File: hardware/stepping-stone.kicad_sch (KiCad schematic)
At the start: 0 parts

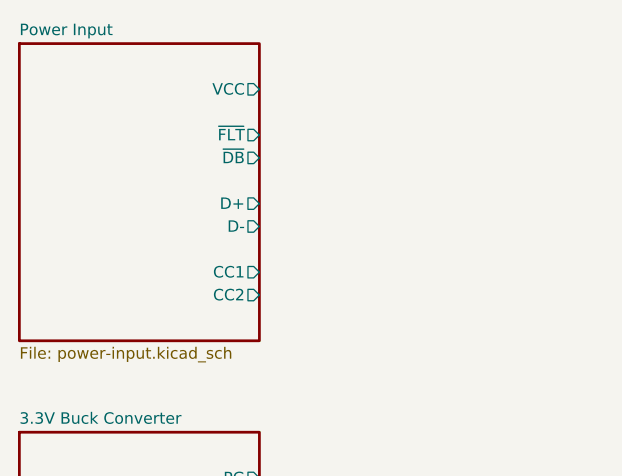
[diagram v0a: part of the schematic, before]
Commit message: Remove USB C PD and refine power input
Deleted USB C PD features due to complexity. Simplified power input schematic. Sourced PSU, connectors, crimps, and created external harness schematics.
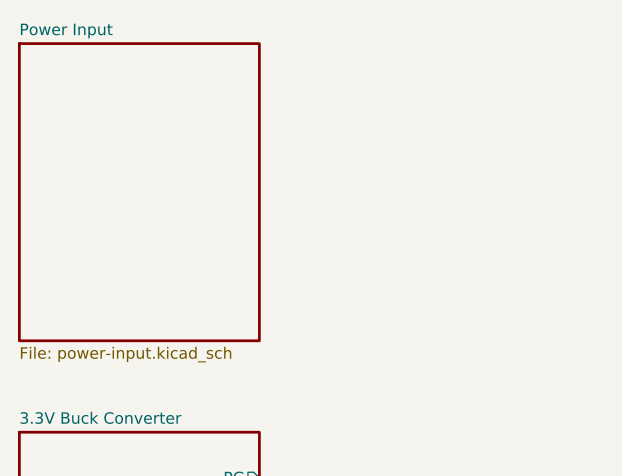
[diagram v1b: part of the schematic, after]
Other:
- sheet Power Input ports: added none; removed CC1, CC2, D+, D-, VCC, ~{DB}, ~{FLT}
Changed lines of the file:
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@@
-			)
-		)
-		(pin "CC1" output
-			(at 68.58 50.8 0)
-			(effects
-				(font
-					(size 1.27 1.27)
-				)
-				(justify right)
-			)
-		)
-		(pin "CC2" output
-			(at 68.58 53.34 0)
-			(effects
-				(font
-					(size 1.27 1.27)
-				)
-				(justify right)
-			)
-		)
-		(pin "D+" output
-			(at 68.58 43.18 0)
-			(effects
-				(font
-					(size 1.27 1.27)
-				)
-				(justify right)
-			)
-		)
-		(pin "D-" output
-			(at 68.58 45.72 0)
-			(effects
-				(font
-					(size 1.27 1.27)
-				)
-				(justify right)
-			)
-		)
-		(pin "VCC" output
-			(at 68.58 30.48 0)
-			(effects
-				(font
-					(size 1.27 1.27)
-				)
-				(justify right)
-			)
-		)
-		(pin "~{DB}" output
-			(at 68.58 38.1 0)
-			(effects
-				(font
-					(size 1.27 1.27)
-				)
-				(justify right)
-			)
-		)
-		(pin "~{FLT}" output
-			(at 68.58 35.56 0)
-			(effects
-				(font
-					(size 1.27 1.27)
-				)
-				(justify right)
 			)
 		)

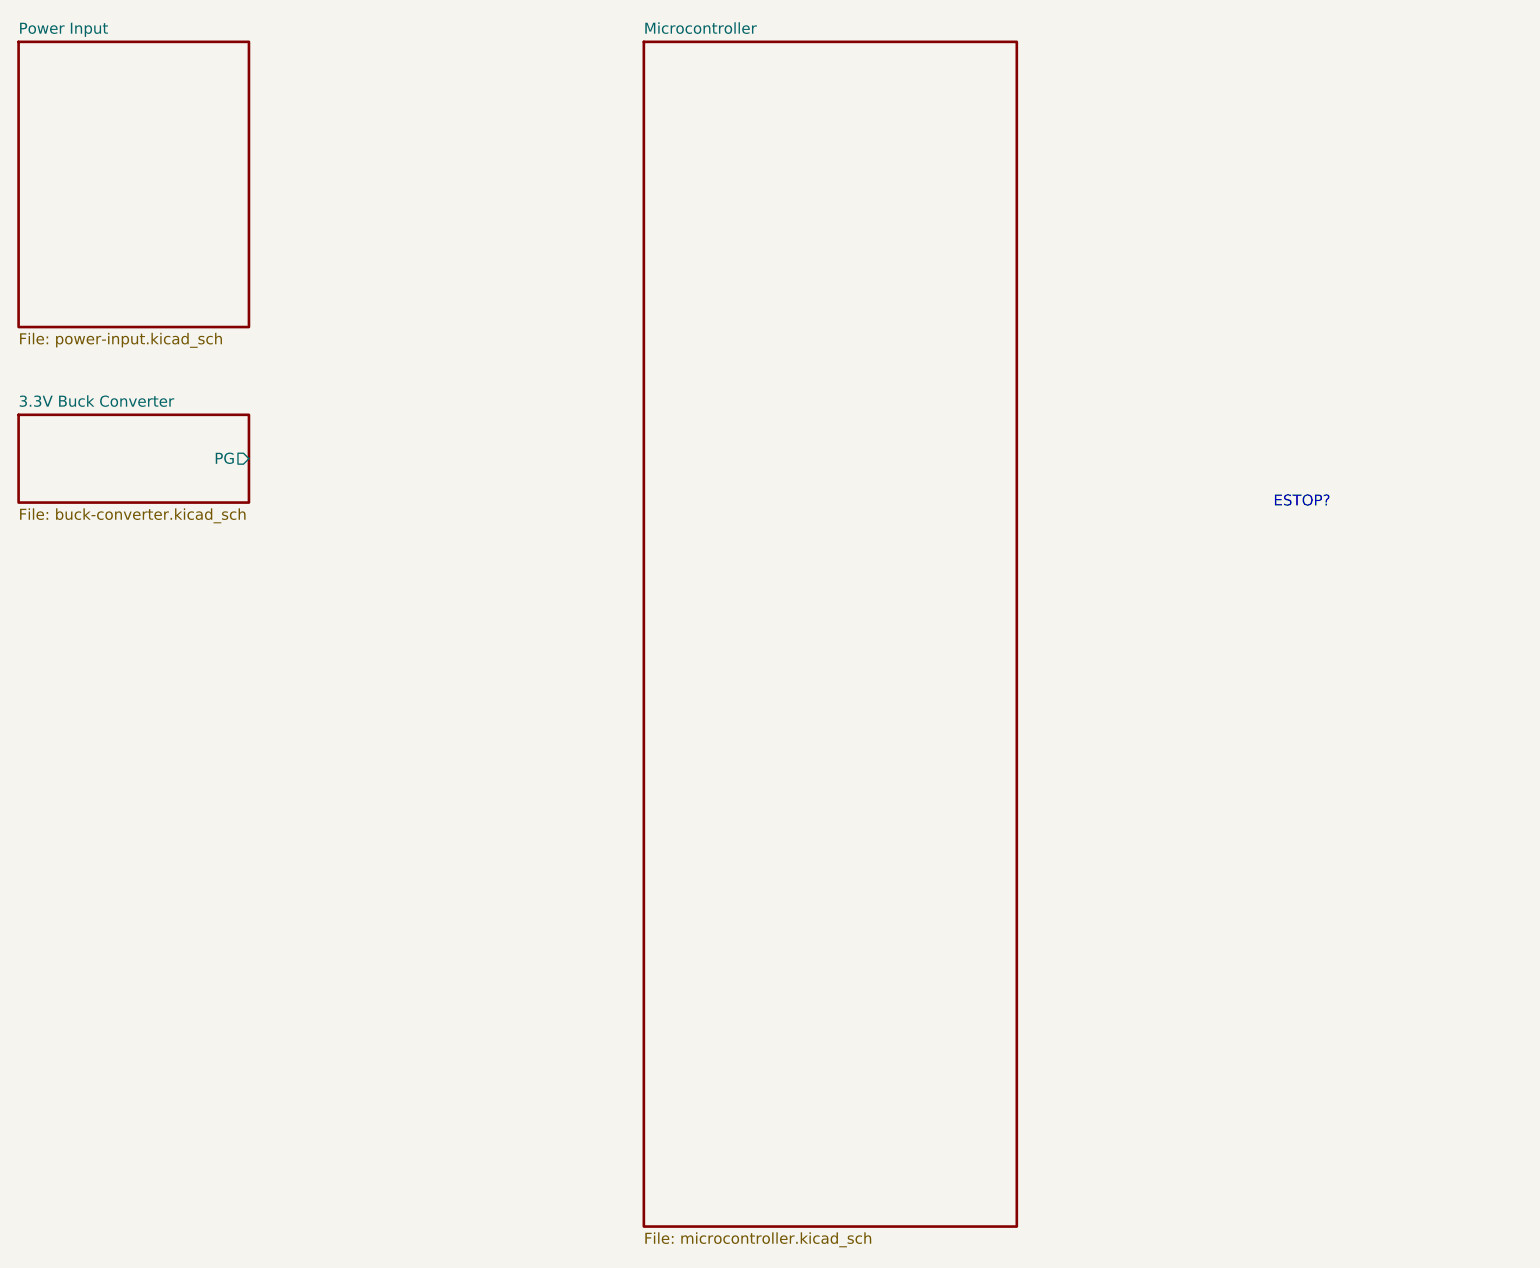
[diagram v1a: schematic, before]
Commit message: Added USB and began estop
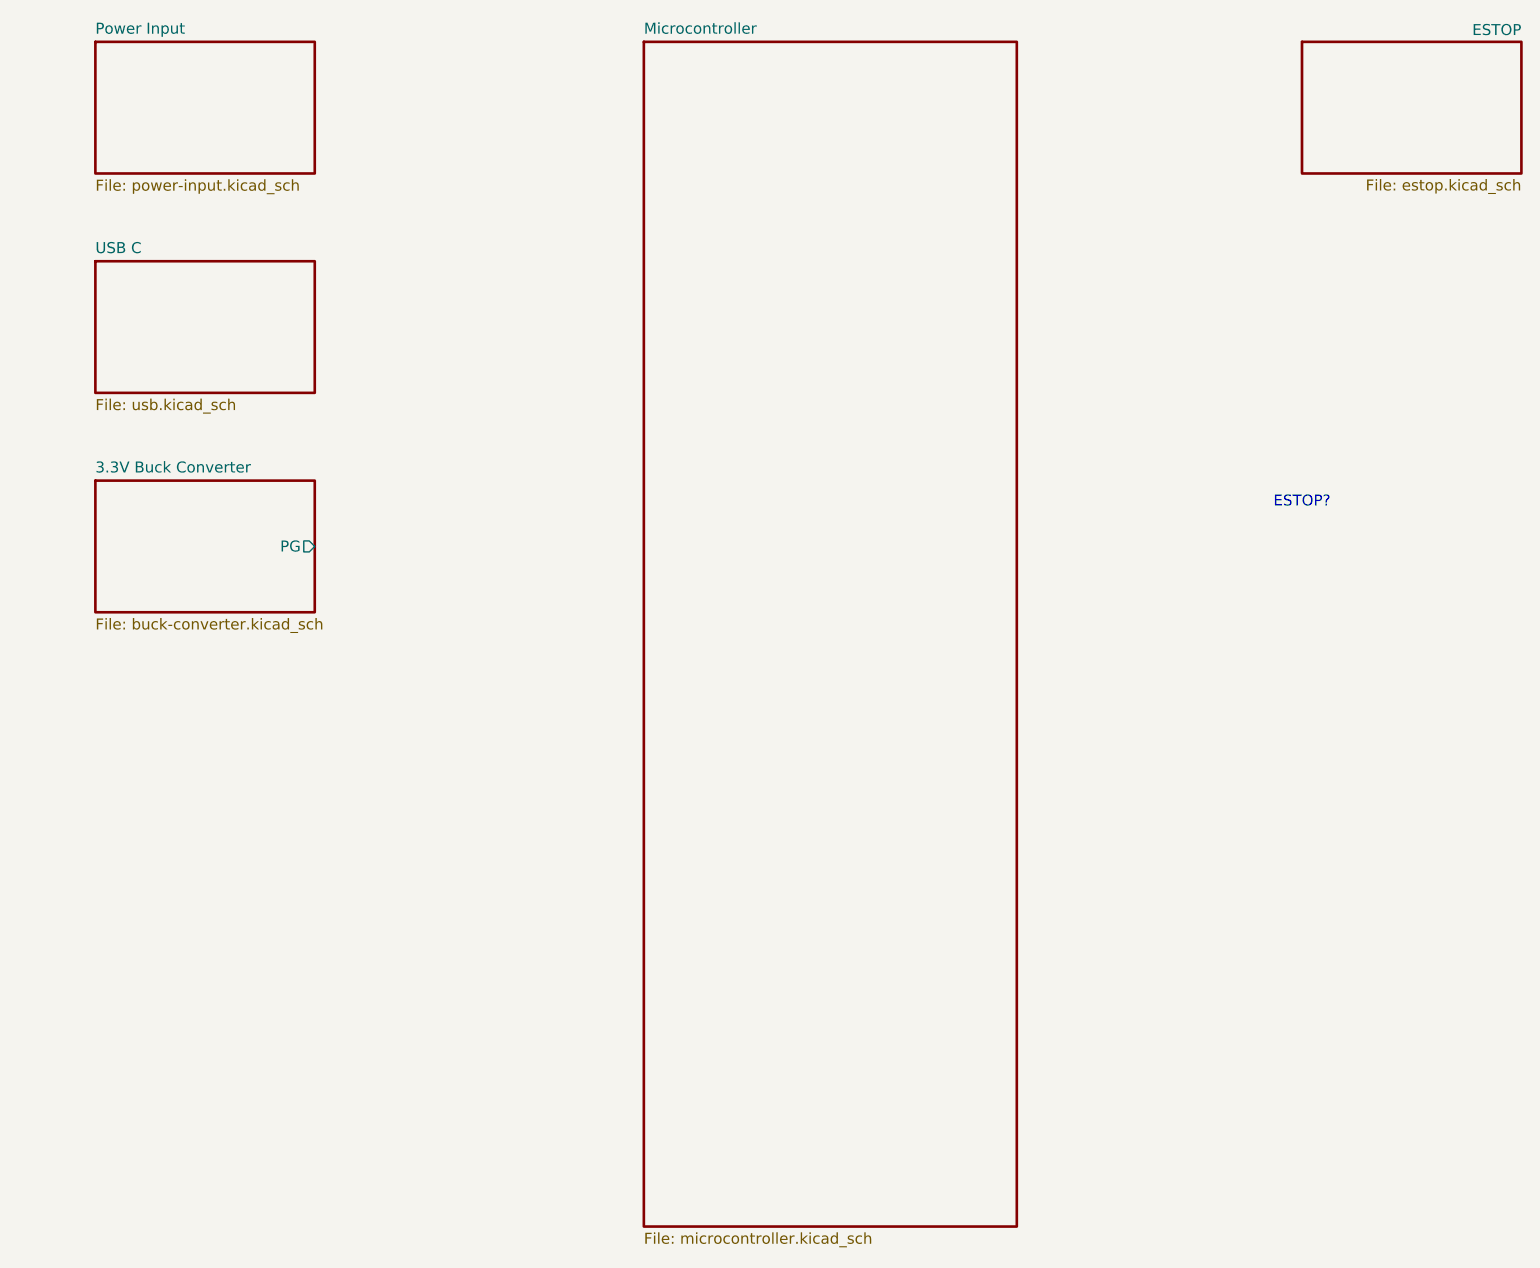
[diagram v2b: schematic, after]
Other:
- added sheet ESTOP (estop.kicad_sch)
- added sheet USB C (usb.kicad_sch)
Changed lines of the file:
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@@
 	)
 	(sheet
-		(at 41.91 25.4)
-		(size 26.67 33.02)
+		(at 50.8 50.8)
+		(size 25.4 15.24)
+		(exclude_from_sim no)
+		(in_bom yes)
+		(on_board yes)
+		(dnp no)
+		(fields_autoplaced yes)
+		(stroke
+			(width 0.3048)
+			(type solid)
+		)
+		(fill
+			(color 255 229 191 1)
+		)
+		(property "Sheetname" "USB C"
+			(at 50.8 50.0122 0)
+			(show_name no)
+			(do_not_autoplace no)
+			(effects
+				(font
+					(size 1.27 1.27)
+				)
+				(justify left bottom)
+			)
+		)
+		(property "Sheetfile" "usb.kicad_sch"
+			(at 50.8 66.7008 0)
+			(show_name no)
+			(do_not_autoplace no)
+			(effects
+				(font
+					(size 1.27 1.27)
+				)
+				(justify left top)
+			)
+		)
+		(instances
+			(project "stepping-stone"
+				(path "/793a882e-3f7b-468b-a863-41a1f527e1bf"
+					(page "5")
+				)
+			)
+		)
+	)
+	(sheet
+		(at 50.8 25.4)
+		(size 25.4 15.24)
 		(exclude_from_sim no)
 		(in_bom yes)
@@
 		)
 		(property "Sheetname" "Power Input"
-			(at 41.91 24.6122 0)
+			(at 50.8 24.6122 0)
 			(show_name no)
 			(do_not_autoplace no)
@@
 		)
 		(property "Sheetfile" "power-input.kicad_sch"
-			(at 41.91 59.0808 0)
+			(at 50.8 41.3008 0)
 			(show_name no)
 			(do_not_autoplace no)
@@
 				(path "/793a882e-3f7b-468b-a863-41a1f527e1bf"
 					(page "3")
+				)
+			)
+		)
+	)
+	(sheet
+		(at 190.5 25.4)
+		(size 25.4 15.24)
+		(exclude_from_sim no)
+		(in_bom yes)
+		(on_board yes)
+		(dnp no)
+		(stroke
+			(width 0.3048)
+			(type solid)
+		)
+		(fill
+			(color 255 229 191 1)
+		)
+		(property "Sheetname" "ESTOP"
+			(at 215.9 24.765 0)
+			(show_name no)
+			(do_not_autoplace no)
+			(effects
+				(font
+					(size 1.27 1.27)
+				)
+				(justify right bottom)
+			)
+		)
+		(property "Sheetfile" "estop.kicad_sch"
+			(at 215.9 41.275 0)
+			(show_name no)
+			(do_not_autoplace no)
+			(effects
+				(font
+					(size 1.27 1.27)
+				)
+				(justify right top)
+			)
+		)
+		(instances
+			(project "stepping-stone"
+				(path "/793a882e-3f7b-468b-a863-41a1f527e1bf"
+					(page "6")
 				)
 			)
@@
 	)
 	(sheet
-		(at 41.91 68.58)
-		(size 26.67 10.16)
+		(at 50.8 76.2)
+		(size 25.4 15.24)
 		(exclude_from_sim no)
 		(in_bom yes)
@@
 		)
 		(property "Sheetname" "3.3V Buck Converter"
-			(at 41.91 67.7922 0)
+			(at 50.8 75.4122 0)
 			(show_name no)
 			(do_not_autoplace no)
@@
 		)
 		(property "Sheetfile" "buck-converter.kicad_sch"
-			(at 41.91 79.4008 0)
+			(at 50.8 92.1008 0)
 			(show_name no)
 			(do_not_autoplace no)
@@
 		)
 		(pin "PG" output
-			(at 68.58 73.66 0)
-			(effects
-				(font
+			(at 76.2 83.82 0)
+			(effects
+				(font
